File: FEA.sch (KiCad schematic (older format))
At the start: 18 parts

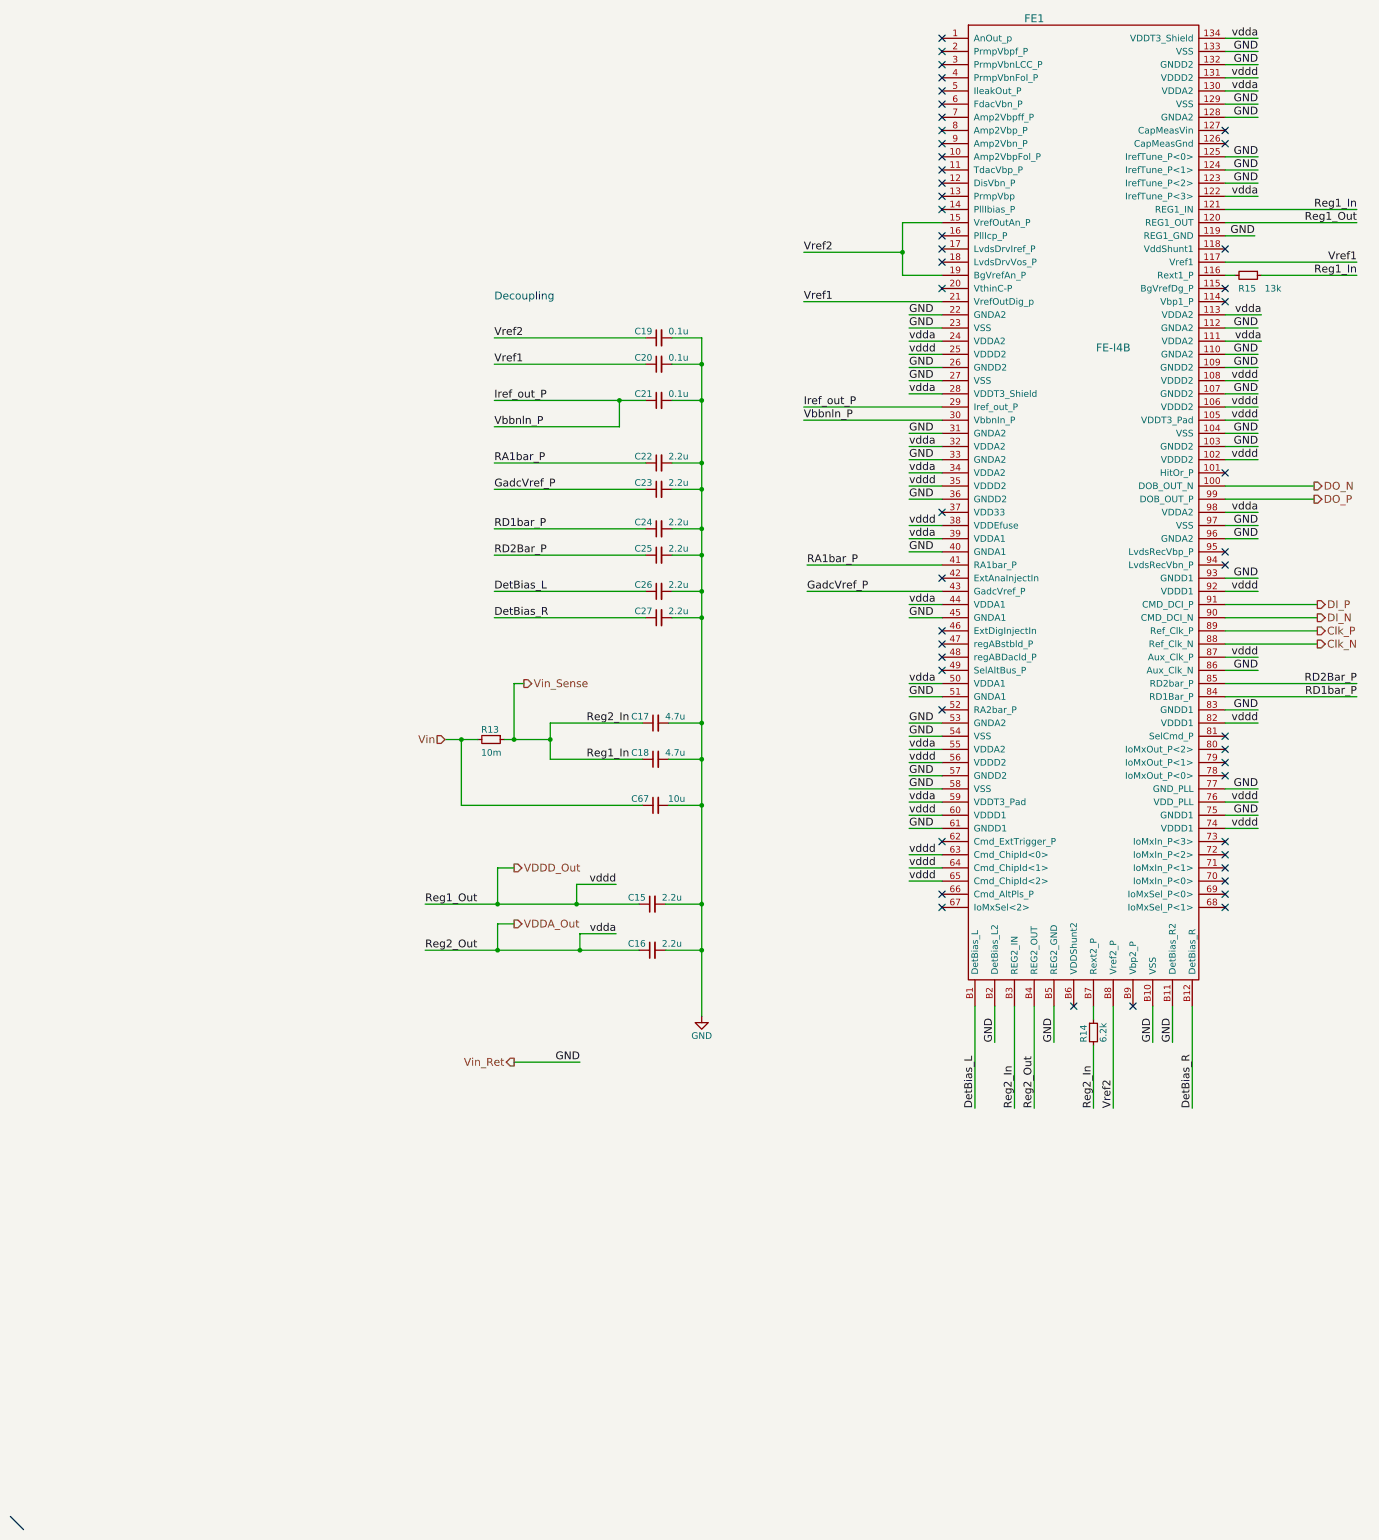
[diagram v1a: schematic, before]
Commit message: Connect analog/digital shunt circuits
Signed-off-by: Katie Dunne <kdunne@mail.ccsf.edu>
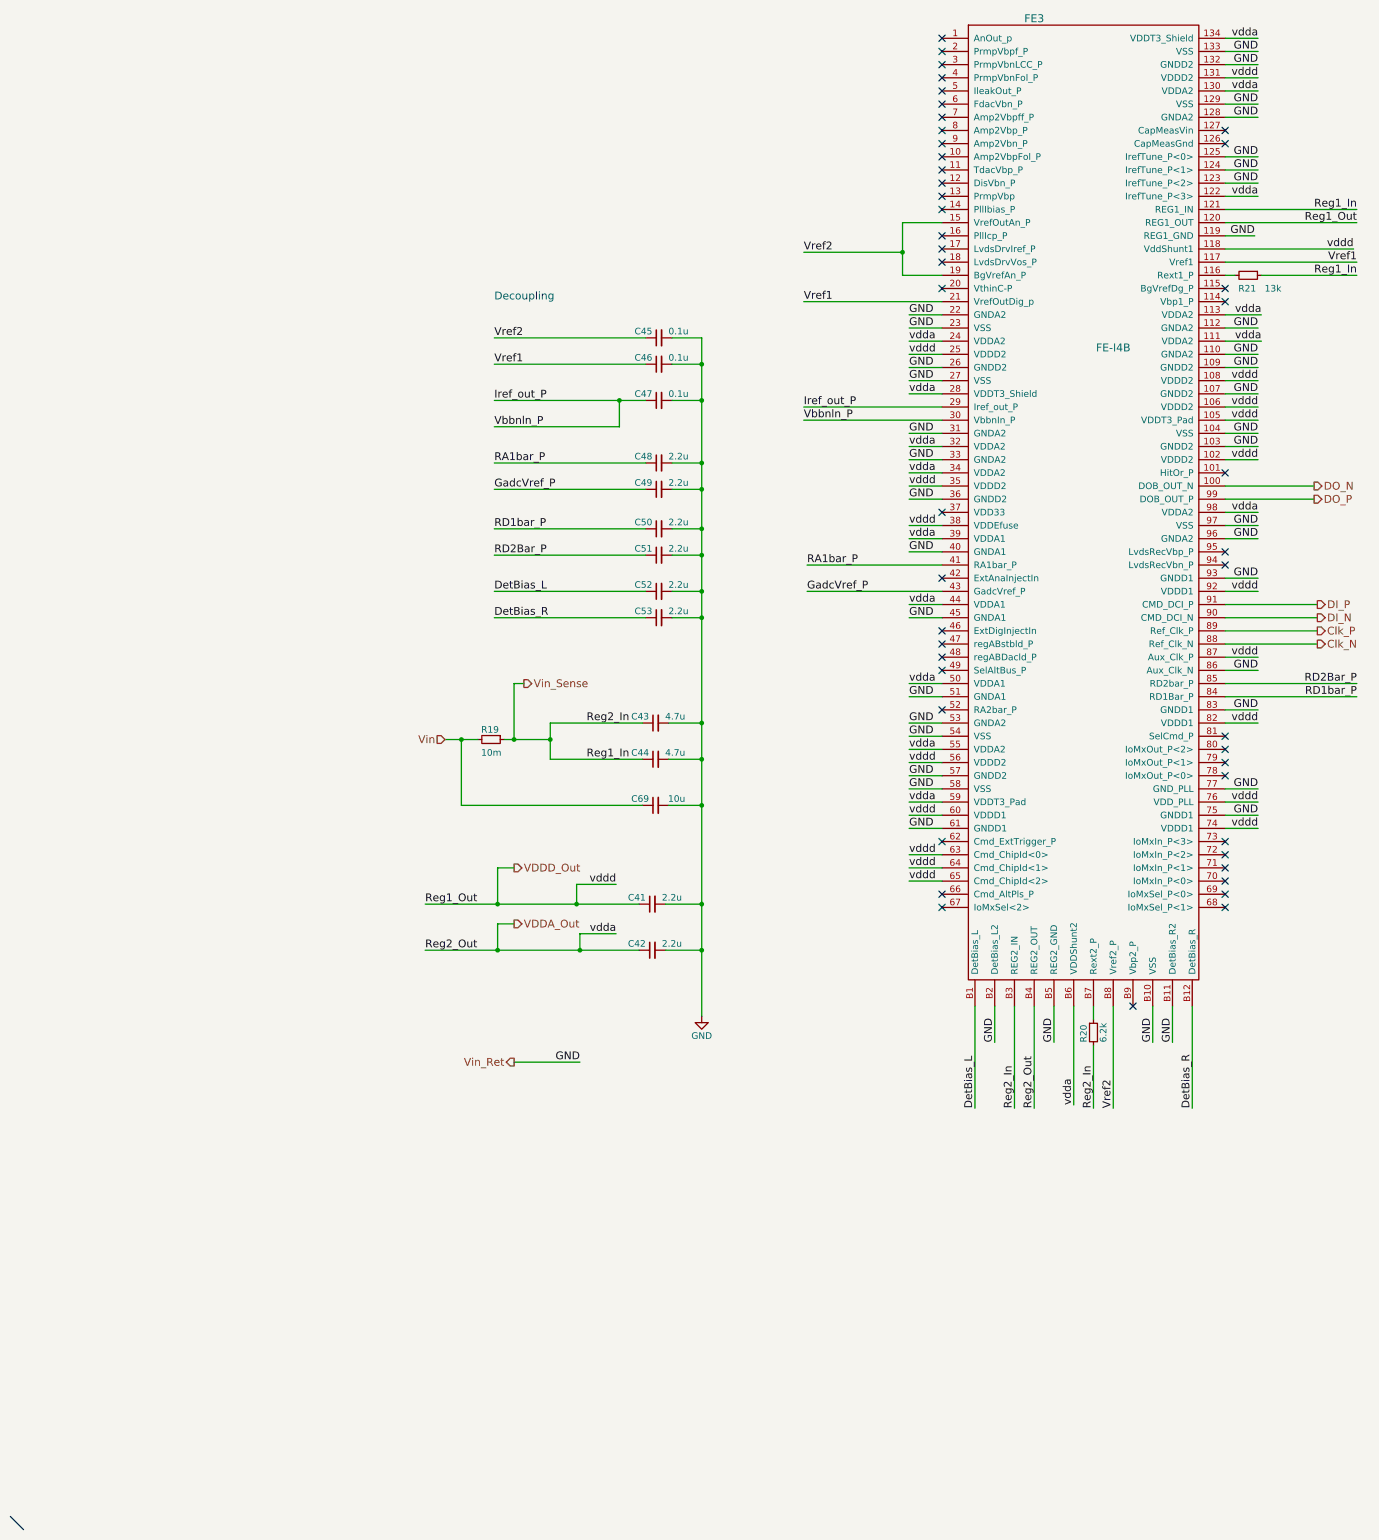
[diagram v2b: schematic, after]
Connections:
- net VDDA_Out: now also FE1.B6 (VDDShunt2)
- net VDDD_Out: now also FE1.118 (VddShunt1)
- no-connect marks 48 -> 46
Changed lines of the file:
@@
 $Descr A4 8268 11693 portrait
 encoding utf-8
-Sheet 2 5
-Title ""
+Sheet 4 5
+Title "FEI4B Quad Module"
 Date ""
-Rev ""
-Comp ""
+Rev "1.2"
+Comp "LBNL"
 Comment1 ""
 Comment2 ""
@@
 AR Path="/58B026BA/589D45EA" Ref="FE3"  Part="1"
 AR Path="/58B026C4/589D45EA" Ref="FE4"  Part="1"
-F 0 "FE1" H 5225 4275 60  0000 C CNN
+F 0 "FE3" H 5225 4275 60  0000 C CNN
 F 1 "FE-I4B" H 5825 1775 60  0000 C CNN
 F 2 "module:WirebondPads" H 5825 2525 60  0001 C CNN
@@
 Text Label 7675 2625 2    59   ~ 0
 Vref1
-NoConn ~ 5525 8275
-NoConn ~ 6675 2525
 NoConn ~ 6675 4225
 NoConn ~ 6675 2825
@@
 AR Path="/58B026BA/58AFC93B" Ref="R20"  Part="1"
 AR Path="/58B026C4/58AFC93B" Ref="R23"  Part="1"
-F 0 "R14" V 5600 8400 50  0000 L CNN
+F 0 "R20" V 5600 8400 50  0000 L CNN
 F 1 "6.2k" V 5750 8400 50  0000 L CNN
 F 2 "Resistors_SMD:R_0402" H 5675 8475 50  0001 C CNN
@@
 AR Path="/58B026BA/58AFD85E" Ref="R21"  Part="1"
 AR Path="/58B026C4/58AFD85E" Ref="R24"  Part="1"
-F 0 "R15" V 6950 2650 50  0000 L CNN
+F 0 "R21" V 6950 2650 50  0000 L CNN
 F 1 "13k" V 6950 2850 50  0000 L CNN
 F 2 "Resistors_SMD:R_0402" H 6850 2725 50  0001 C CNN
@@
 AR Path="/58B026BA/58BA4BDB" Ref="#PWR06"  Part="1"
 AR Path="/58B026C4/58BA4BDB" Ref="#PWR07"  Part="1"
-F 0 "#PWR04" H 2700 8100 50  0001 C CNN
+F 0 "#PWR06" H 2700 8100 50  0001 C CNN
 F 1 "GND" H 2700 8200 50  0000 C CNN
 F 2 "" H 2700 8350 50  0001 C CNN
@@
 AR Path="/58B026BA/58BA843C" Ref="C45"  Part="1"
 AR Path="/58B026C4/58BA843C" Ref="C58"  Part="1"
-F 0 "C19" V 2425 3250 50  0000 L CNN
+F 0 "C45" V 2425 3250 50  0000 L CNN
 F 1 "0.1u" V 2425 2975 50  0000 L CNN
 F 2 "Capacitors_SMD:C_0402" H 2375 3200 50  0001 C CNN
@@
 AR Path="/58B026BA/58B3509B" Ref="R19"  Part="1"
 AR Path="/58B026C4/58B3509B" Ref="R22"  Part="1"
-F 0 "R13" V 1025 6175 50  0000 L CNN
+F 0 "R19" V 1025 6175 50  0000 L CNN
 F 1 "10m" V 1200 6175 50  0000 L CNN
 F 2 "Resistors_SMD:R_0603" H 1100 6250 50  0001 C CNN
@@
 AR Path="/58B026BA/58B81EC6" Ref="C46"  Part="1"
 AR Path="/58B026C4/58B81EC6" Ref="C59"  Part="1"
-F 0 "C20" V 2425 3450 50  0000 L CNN
+F 0 "C46" V 2425 3450 50  0000 L CNN
 F 1 "0.1u" V 2425 3175 50  0000 L CNN
 F 2 "Capacitors_SMD:C_0402" H 2375 3400 50  0001 C CNN
@@
 AR Path="/58B026BA/58B81EFE" Ref="C47"  Part="1"
 AR Path="/58B026C4/58B81EFE" Ref="C60"  Part="1"
-F 0 "C21" V 2425 3725 50  0000 L CNN
+F 0 "C47" V 2425 3725 50  0000 L CNN
 F 1 "0.1u" V 2425 3450 50  0000 L CNN
 F 2 "Capacitors_SMD:C_0402" H 2375 3675 50  0001 C CNN
@@
 AR Path="/58B026BA/58B81F3D" Ref="C48"  Part="1"
 AR Path="/58B026C4/58B81F3D" Ref="C61"  Part="1"
-F 0 "C22" V 2425 4200 50  0000 L CNN
+F 0 "C48" V 2425 4200 50  0000 L CNN
 F 1 "2.2u" V 2425 3925 50  0000 L CNN
 F 2 "Capacitors_SMD:C_0402" H 2375 4150 50  0001 C CNN
@@
 AR Path="/58B026BA/58B81F93" Ref="C49"  Part="1"
 AR Path="/58B026C4/58B81F93" Ref="C62"  Part="1"
-F 0 "C23" V 2425 4400 50  0000 L CNN
+F 0 "C49" V 2425 4400 50  0000 L CNN
 F 1 "2.2u" V 2425 4125 50  0000 L CNN
 F 2 "Capacitors_SMD:C_0402" H 2375 4350 50  0001 C CNN
@@
 AR Path="/58B026BA/58B82007" Ref="C50"  Part="1"
 AR Path="/58B026C4/58B82007" Ref="C63"  Part="1"
-F 0 "C24" V 2425 4700 50  0000 L CNN
+F 0 "C50" V 2425 4700 50  0000 L CNN
 F 1 "2.2u" V 2425 4425 50  0000 L CNN
 F 2 "Capacitors_SMD:C_0402" H 2375 4650 50  0001 C CNN
@@
 AR Path="/58B026BA/58B82049" Ref="C51"  Part="1"
 AR Path="/58B026C4/58B82049" Ref="C64"  Part="1"
-F 0 "C25" V 2425 4900 50  0000 L CNN
+F 0 "C51" V 2425 4900 50  0000 L CNN
 F 1 "2.2u" V 2425 4625 50  0000 L CNN
 F 2 "Capacitors_SMD:C_0402" H 2375 4850 50  0001 C CNN
@@
 AR Path="/58B026BA/58B82086" Ref="C52"  Part="1"
 AR Path="/58B026C4/58B82086" Ref="C65"  Part="1"
-F 0 "C26" V 2425 5175 50  0000 L CNN
+F 0 "C52" V 2425 5175 50  0000 L CNN
 F 1 "2.2u" V 2425 4900 50  0000 L CNN
 F 2 "Capacitors_SMD:C_0402" H 2375 5125 50  0001 C CNN
@@
 AR Path="/58B026BA/58B820CA" Ref="C53"  Part="1"
 AR Path="/58B026C4/58B820CA" Ref="C66"  Part="1"
-F 0 "C27" V 2425 5375 50  0000 L CNN
+F 0 "C53" V 2425 5375 50  0000 L CNN
 F 1 "2.2u" V 2425 5100 50  0000 L CNN
 F 2 "Capacitors_SMD:C_0402" H 2375 5325 50  0001 C CNN
@@
 AR Path="/58B026BA/58B82111" Ref="C43"  Part="1"
 AR Path="/58B026C4/58B82111" Ref="C56"  Part="1"
-F 0 "C17" V 2400 6175 50  0000 L CNN
+F 0 "C43" V 2400 6175 50  0000 L CNN
 F 1 "4.7u" V 2400 5900 50  0000 L CNN
 F 2 "Capacitors_SMD:C_0402" H 2350 6125 50  0001 C CNN
@@
 AR Path="/58B026BA/58B82175" Ref="C44"  Part="1"
 AR Path="/58B026C4/58B82175" Ref="C57"  Part="1"
-F 0 "C18" V 2400 6450 50  0000 L CNN
+F 0 "C44" V 2400 6450 50  0000 L CNN
 F 1 "4.7u" V 2400 6175 50  0000 L CNN
 F 2 "Capacitors_SMD:C_0402" H 2350 6400 50  0001 C CNN
@@
 AR Path="/58B026BA/58B8280B" Ref="C41"  Part="1"
 AR Path="/58B026C4/58B8280B" Ref="C54"  Part="1"
-F 0 "C15" V 2375 7550 50  0000 L CNN
+F 0 "C41" V 2375 7550 50  0000 L CNN
 F 1 "2.2u" V 2375 7275 50  0000 L CNN
 F 2 "Capacitors_SMD:C_0402" H 2325 7500 50  0001 C CNN
@@
 AR Path="/58B026BA/58B82875" Ref="C42"  Part="1"
 AR Path="/58B026C4/58B82875" Ref="C55"  Part="1"
-F 0 "C16" V 2375 7900 50  0000 L CNN
+F 0 "C42" V 2375 7900 50  0000 L CNN
 F 1 "2.2u" V 2375 7625 50  0000 L CNN
 F 2 "Capacitors_SMD:C_0402" H 2325 7850 50  0001 C CNN
@@
 AR Path="/58B026BA/58C23965" Ref="C69"  Part="1"
 AR Path="/58B026C4/58C23965" Ref="C70"  Part="1"
-F 0 "C67" V 2400 6800 50  0000 L CNN
+F 0 "C69" V 2400 6800 50  0000 L CNN
 F 1 "10u" V 2400 6525 50  0000 L CNN
 F 2 "Capacitors_SMD:C_0603" H 2350 6750 50  0001 C CNN
@@
 Text Label 1775 8700 2    59   ~ 0
 GND
+Text Label 5525 9025 1    59   ~ 0
+vdda
+Text Label 7650 2525 2    59   ~ 0
+vddd
+Wire Wire Line
+	6675 2525 7650 2525
+Wire Wire Line
+	5525 9025 5525 8275
 $EndSCHEMATC
